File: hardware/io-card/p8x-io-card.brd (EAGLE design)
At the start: 160 x 100 mm, 56 parts, among them J1 FABC96R, J2 SERIAL, J3 RTC 3-WIRE, SW1 INPUT, U1 IO PAGE, U10 LED PORT, U11 MON A-LO, U12 MON A-HI, U13 MON D, U14 ACIA, U15 74HCT00, U16 RTC DNP, U2 PORT DEC, U3 DOE DEC, U4 DLD DEC, U5 74HCT32, U6 74HCT08, U7 BAUD DIV, U8 RS232, U9 SW IN, X2 2.4576MHZ, X3 32.768KHZ

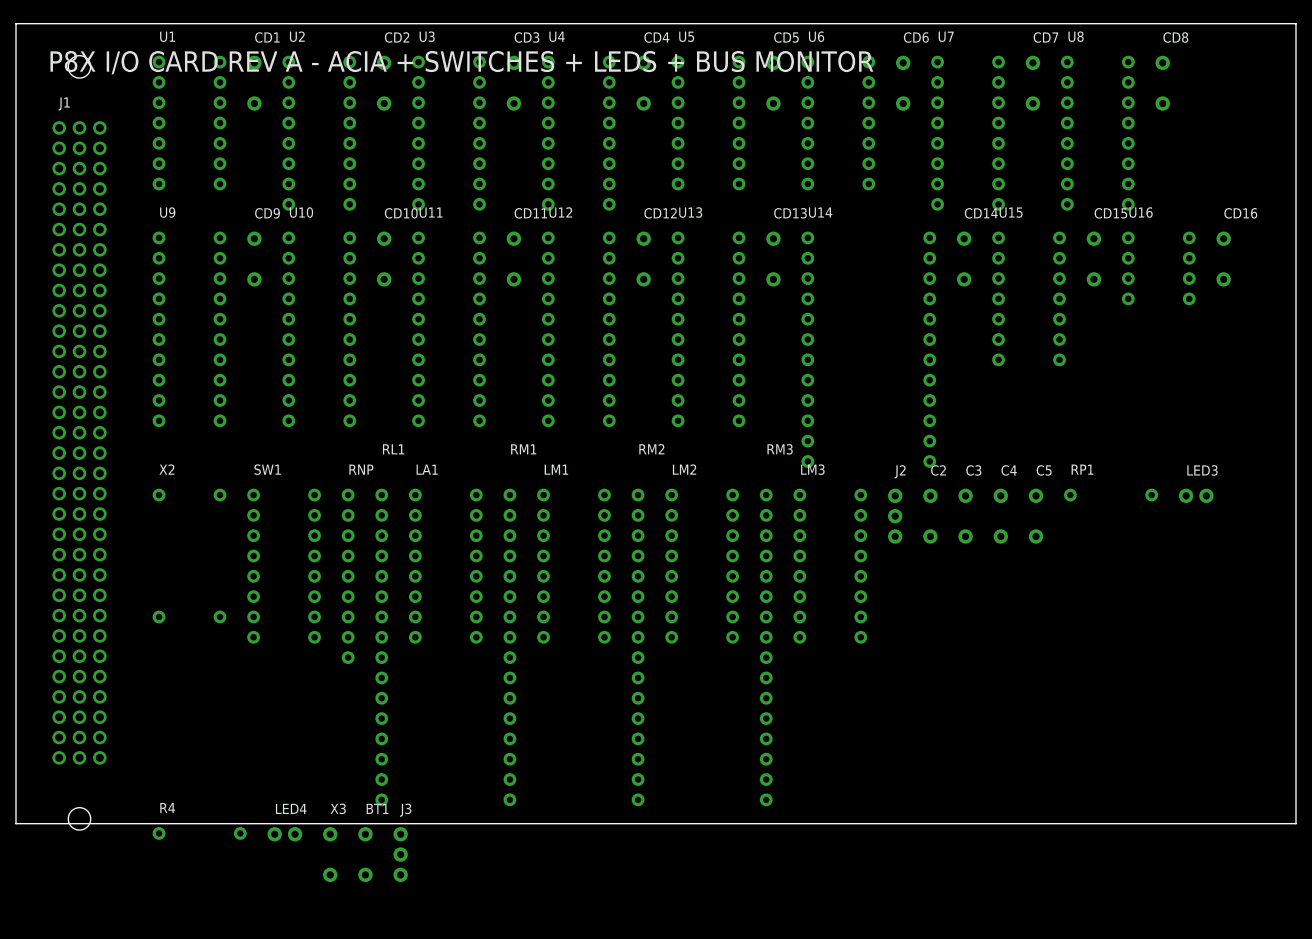
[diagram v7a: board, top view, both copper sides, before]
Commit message: feat(generators): faithful Eagle/Fusion output (values, layers, smashed parts)
Make the generated .sch/.brd match how Eagle itself writes files, so Fusion
displays everything correctly (was mis-mapping names/values to scratch layers):

- devicesets get uservalue="yes" so the `value` field is honored at all (it was
  silently ignored before — no card's value ever displayed)
- emit the COMPLETE standard Eagle layer table (62 layers) in every drawing, so
  Fusion has nothing to remap on import
- board elements are now smashed="yes" with explicit NAME (tNames/25) and VALUE
  (tValues/27) attributes — refdes + part number show reliably
- add std <attributes>/<variantdefs> board sections + board-package >VALUE silk
- schematic: `value` holds the orderable part number (>VALUE + BOM); the logical
  function is placed as text near each chip via a new card() `labels` arg
- write_brd gains outline_only and unplaced modes (parts off-board + ratsnest);
  card() exposes brd_outline_only / brd_unplaced

Proven on the LED card (part numbers + function labels + an unplaced 4-layer
board). The other cards get the structural fixes now; rolling the part-number/
labels convention across them is the next step. All 8 boards validate (0 errors).

Co-Authored-By: Claude Opus 4.8 <noreply@anthropic.com>
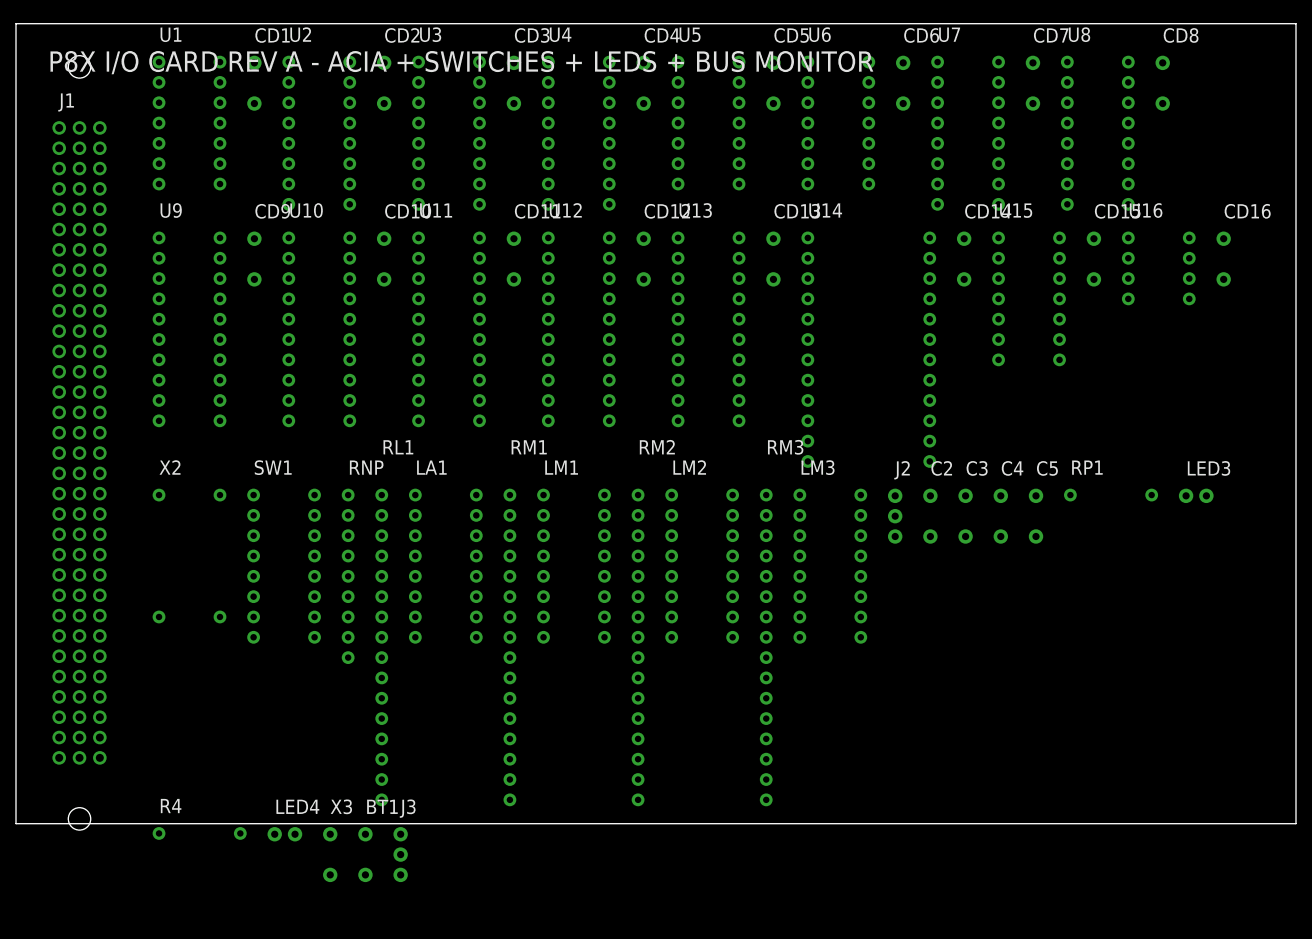
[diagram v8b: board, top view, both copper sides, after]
